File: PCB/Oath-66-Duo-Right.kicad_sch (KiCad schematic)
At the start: 67 parts, among them U2 Arduino_Pro_Micro

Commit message: PCB Updated
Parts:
- S52: footprint ScottoKeebs_Hotswap:Hotswap_MX_1.50u -> ScottoKeebs_Hotswap:Hotswap_MX_1.00u
- S53: footprint ScottoKeebs_Hotswap:Hotswap_MX_1.00u -> ScottoKeebs_Hotswap:Hotswap_MX_1.50u
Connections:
- net Col 0: no longer D48.1 (K), D49.1 (K), D50.1 (K), D51.1 (K), D52.1 (K), D53.1 (K), U2.12 (9/PB5)
- net Col 1: now also S62.1
- net Col 2: no longer S62.1
- new net Row 2: D48.1 (K), D49.1 (K), D50.1 (K), D51.1 (K), D52.1 (K), D53.1 (K), U2.12 (9/PB5)
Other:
- moved on the sheet: D62, S62
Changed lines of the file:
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@@
 	)
 	(junction
-		(at 189.23 101.6)
-		(diameter 0)
-		(color 0 0 0 0)
-	)
-	(junction
 		(at 234.95 48.26)
 		(diameter 0)
@@
 	)
 	(junction
-		(at 212.09 109.22)
-		(diameter 0)
-		(color 0 0 0 0)
-	)
-	(junction
 		(at 234.95 109.22)
 		(diameter 0)
@@
 	)
 	(junction
+		(at 200.66 109.22)
+		(diameter 0)
+		(color 0 0 0 0)
+	)
+	(junction
 		(at 240.03 121.92)
 		(diameter 0)
@@
 	)
 	(junction
+		(at 205.74 142.24)
+		(diameter 0)
+		(color 0 0 0 0)
+	)
+	(junction
 		(at 240.03 101.6)
 		(diameter 0)
@@
 	)
 	(junction
-		(at 217.17 142.24)
-		(diameter 0)
-		(color 0 0 0 0)
-	)
-	(junction
 		(at 234.95 68.58)
 		(diameter 0)
@@
 	)
 	(junction
-		(at 205.74 101.6)
-		(diameter 0)
-		(color 0 0 0 0)
-	)
-	(junction
 		(at 257.81 68.58)
 		(diameter 0)
@@
 	(wire
 		(pts
-			(xy 251.46 142.24) (xy 262.89 142.24)
+			(xy 200.66 109.22) (xy 200.66 129.54)
 		)
 		(stroke
@@
 	(wire
 		(pts
-			(xy 228.6 121.92) (xy 240.03 121.92)
+			(xy 251.46 142.24) (xy 262.89 142.24)
 		)
 		(stroke
@@
 	(wire
 		(pts
-			(xy 194.31 142.24) (xy 217.17 142.24)
+			(xy 228.6 121.92) (xy 240.03 121.92)
 		)
 		(stroke
@@
 	(wire
 		(pts
-			(xy 212.09 48.26) (xy 212.09 68.58)
+			(xy 194.31 142.24) (xy 205.74 142.24)
 		)
 		(stroke
@@
 	(wire
 		(pts
-			(xy 194.31 121.92) (xy 205.74 121.92)
+			(xy 212.09 48.26) (xy 212.09 68.58)
 		)
 		(stroke
@@
 	(wire
 		(pts
-			(xy 217.17 142.24) (xy 228.6 142.24)
+			(xy 194.31 121.92) (xy 205.74 121.92)
 		)
 		(stroke
@@
 	(wire
 		(pts
-			(xy 246.38 88.9) (xy 246.38 109.22)
+			(xy 205.74 142.24) (xy 228.6 142.24)
 		)
 		(stroke
@@
 	(wire
 		(pts
-			(xy 189.23 101.6) (xy 205.74 101.6)
+			(xy 246.38 88.9) (xy 246.38 109.22)
 		)
 		(stroke
@@
 	(wire
 		(pts
-			(xy 189.23 68.58) (xy 189.23 101.6)
-		)
-		(stroke
-			(width 0)
-			(type default)
-		)
-	)
-	(wire
-		(pts
 			(xy 88.9 62.23) (xy 86.36 62.23)
 		)
@@
 	(wire
 		(pts
-			(xy 189.23 101.6) (xy 189.23 109.22)
+			(xy 189.23 68.58) (xy 189.23 109.22)
 		)
 		(stroke
@@
 	(wire
 		(pts
-			(xy 212.09 109.22) (xy 212.09 129.54)
-		)
-		(stroke
-			(width 0)
-			(type default)
-		)
-	)
-	(wire
-		(pts
 			(xy 205.74 101.6) (xy 217.17 101.6)
 		)
@@
 	(symbol
 		(lib_id "ScottoKeebs:Placeholder_Keyswitch")
-		(at 214.63 132.08 0)
+		(at 203.2 132.08 0)
 		(unit 1)
 		(exclude_from_sim no)
@@
 		(fields_autoplaced yes)
 		(property "Reference" "S62"
-			(at 214.63 124.46 0)
+			(at 203.2 124.46 0)
 			(effects
 				(font
@@
 		)
 		(property "Value" "Keyswitch"
-			(at 214.63 127 0)
+			(at 203.2 127 0)
 			(effects
 				(font
@@
 		)
 		(property "Footprint" "ScottoKeebs_Hotswap:Hotswap_MX_2.00u"
-			(at 214.63 132.08 0)
+			(at 203.2 132.08 0)
 			(effects
 				(font
@@
 		)
 		(property "Datasheet" "~"
-			(at 214.63 132.08 0)
+			(at 203.2 132.08 0)
 			(effects
 				(font
@@
 		)
 		(property "Description" "Push button switch, normally open, two pins, 45° tilted"
-			(at 214.63 132.08 0)
+			(at 203.2 132.08 0)
 			(effects
 				(font
@@
 	(symbol
 		(lib_id "ScottoKeebs:Placeholder_Diode")
-		(at 217.17 138.43 90)
+		(at 205.74 138.43 90)
 		(unit 1)
 		(exclude_from_sim no)
@@
 		(fields_autoplaced yes)
 		(property "Reference" "D62"
-			(at 219.71 137.1599 90)
+			(at 208.28 137.1599 90)
 			(effects
 				(font
@@
 		)
 		(property "Value" "Diode"
-			(at 219.71 139.6999 90)
+			(at 208.28 139.6999 90)
 			(effects
 				(font
@@
 		)
 		(property "Footprint" "ScottoKeebs_Components:Diode_SOD-123"
-			(at 217.17 138.43 0)
+			(at 205.74 138.43 0)
 			(effects
 				(font
@@
 		)
 		(property "Datasheet" ""
-			(at 217.17 138.43 0)
+			(at 205.74 138.43 0)
 			(effects
 				(font
@@
 		)
 		(property "Description" "1N4148 (DO-35) or 1N4148W (SOD-123)"
-			(at 217.17 138.43 0)
+			(at 205.74 138.43 0)
 			(effects
 				(font
@@
 		)
 		(property "Sim.Device" "D"
-			(at 217.17 138.43 0)
+			(at 205.74 138.43 0)
 			(effects
 				(font
@@
 		)
 		(property "Sim.Pins" "1=K 2=A"
-			(at 217.17 138.43 0)
+			(at 205.74 138.43 0)
 			(effects
 				(font
@@
 			)
 		)
-		(property "Footprint" "ScottoKeebs_Hotswap:Hotswap_MX_1.00u"
+		(property "Footprint" "ScottoKeebs_Hotswap:Hotswap_MX_1.50u"
 			(at 260.35 91.44 0)
 			(effects
@@
 			)
 		)
-		(property "Footprint" "ScottoKeebs_Hotswap:Hotswap_MX_1.50u"
+		(property "Footprint" "ScottoKeebs_Hotswap:Hotswap_MX_1.00u"
 			(at 248.92 91.44 0)
 			(effects

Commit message: PCB Updated
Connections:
- net Col 0: now also U2.9 (6/PD7); no longer U2.8 (5/PC6)
- net Col 1: now also U2.20 (A3/PF4); no longer U2.10 (7/PE6)
- net Col 2: now also U2.18 (A1/PF6); no longer U2.11 (8/PB4)
- net Col 3: now also U2.16 (15/PB1); no longer U2.15 (14/PB3)
- net Col 4: now also U2.14 (16/PB2); no longer U2.13 (10/PB6)
- net Col 5: now also U2.12 (9/PB5); no longer U2.5 (2/PD1)
- net Col 6: now also U2.11 (8/PB4); no longer U2.6 (3/PD0)
- net Row 0: now also U2.10 (7/PE6); no longer U2.7 (4/PD4)
- net Row 1: now also U2.19 (A2/PF5); no longer U2.9 (6/PD7)
- net Row 2: now also U2.17 (A0/PF7); no longer U2.12 (9/PB5)
- net Row 3: now also U2.15 (14/PB3); no longer U2.16 (15/PB1)
- net Row 4: now also U2.13 (10/PB6); no longer U2.14 (16/PB2)

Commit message: PCB Updated
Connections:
- net Col 0: now also U2.10 (7/PE6); no longer U2.9 (6/PD7)
- net Col 1: now also U2.9 (6/PD7); no longer U2.20 (A3/PF4)
- net Col 2: now also U2.14 (16/PB2); no longer U2.18 (A1/PF6)
- net Col 4: now also U2.18 (A1/PF6); no longer U2.14 (16/PB2)
- net Col 5: now also U2.20 (A3/PF4); no longer U2.12 (9/PB5)
- net Row 0: now also U2.12 (9/PB5); no longer U2.10 (7/PE6)

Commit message: Schematic and PCB Updated
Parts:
- added H10, H6, H7, H8, H9: Mounting_Hole, MountingHole:MountingHole_2.5mm, symbol ScottoKeebs:Placeholder_Mounting_Hole
- added J2: Conn_01x02, Connector_JST:JST_PH_S2B-PH-K_1x02_P2.00mm_Horizontal, symbol Connector_Generic:Conn_01x02
- added PSW2: ~, MyLibrary:MSK_1134_3PIN_2H, symbol MyLibrary:MSK_1134_3PIN_2H
- added RSW2: ~, MyLibrary:Tactile_Switch_3_6_2.5mm, symbol MyLibrary:Tactile_Swtich_3*6*2.5mm
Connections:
- net BAT+_R: now reaches U2.21 (VCC)
- net BAT+_R: now also PSW2.2
- net RST_R: now reaches U2.22 (RST)
- net RST_R: now also RSW2.1
- net GND_R: now reaches U2.3 (GND)
- net GND_R: now also U2.4 (GND), J2.2 (Pin_2), RSW2.2
- net Col 0 renamed COL0_R
- net Col 1 renamed COL1_R
- net Col 2 renamed COL2_R
- net Col 3 renamed COL3_R
- net Col 4 renamed COL4_R
- net Col 5 renamed COL5_R
- net Col 6 renamed COL6_R
- net Row 0 renamed ROW0_R
- net Row 1 renamed ROW1_R
- net Row 2 renamed ROW2_R
- net Row 3 renamed ROW3_R
- net Row 4 renamed ROW4_R
- new net VBAT_R: J2.1 (Pin_1), PSW2.3
- no-connect marks 0 -> 9

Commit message: PCB Routing Finished
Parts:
- removed J2: Conn_01x02, Connector_JST:JST_PH_S2B-PH-K_1x02_P2.00mm_Horizontal, symbol Connector_Generic:Conn_01x02
- added J2: Connector_PH2.0_2Pin_Horizontal, Connector_JST:JST_GH_SM02B-GHS-TB_1x02-1MP_P1.25mm_Horizontal, symbol MyLibrary:Connector_PH2.0_2Pin_Horizontal
- PSW2: footprint MyLibrary:MSK_1134_3PIN_2H -> MyLibrary:MSK_1134_3Pin_2H; symbol MyLibrary:MSK_1134_3PIN_2H -> MyLibrary:MSK_1134_3Pin_2H
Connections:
- net GND_R: now also U2.23 (GND), J2.2 (Pin_2)
- net VBAT_R: now also J2.1 (Pin_1)
- no-connect marks 9 -> 10
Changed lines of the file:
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@@
 	)
 	(no_connect
-		(at 86.36 44.45)
-	)
-	(no_connect
 		(at 55.88 52.07)
 	)
@@
 	)
 	(no_connect
+		(at 139.7 93.98)
+	)
+	(no_connect
 		(at 146.05 55.88)
 	)
@@
 	)
 	(no_connect
+		(at 139.7 81.28)
+	)
+	(no_connect
 		(at 55.88 54.61)
 	)
@@
 	(wire
 		(pts
+			(xy 88.9 44.45) (xy 86.36 44.45)
+		)
+		(stroke
+			(width 0)
+			(type default)
+		)
+	)
+	(wire
+		(pts
 			(xy 234.95 109.22) (xy 234.95 129.54)
 		)
@@
 		)
 	)
+	(hierarchical_label "GND_R"
+		(shape input)
+		(at 88.9 44.45 0)
+		(effects
+			(font
+				(size 1.27 1.27)
+			)
+			(justify left)
+		)
+	)
 	(hierarchical_label "ROW0_R"
 		(shape input)
@@
 	)
 	(symbol
-		(lib_id "Connector_Generic:Conn_01x02")
-		(at 139.7 88.9 180)
-		(unit 1)
-		(exclude_from_sim no)
-		(in_bom yes)
-		(on_board yes)
-		(dnp no)
-		(fields_autoplaced yes)
-		(property "Reference" "J2"
-			(at 139.7 80.01 0)
-			(effects
-				(font
-					(size 1.27 1.27)
-				)
-			)
-		)
-		(property "Value" "Conn_01x02"
-			(at 139.7 82.55 0)
-			(effects
-				(font
-					(size 1.27 1.27)
-				)
-			)
-		)
-		(property "Footprint" "Connector_JST:JST_PH_S2B-PH-K_1x02_P2.00mm_Horizontal"
-			(at 139.7 88.9 0)
-			(effects
-				(font
-					(size 1.27 1.27)
-				)
-				(hide yes)
-			)
-		)
-		(property "Datasheet" "~"
-			(at 139.7 88.9 0)
-			(effects
-				(font
-					(size 1.27 1.27)
-				)
-				(hide yes)
-			)
-		)
-		(property "Description" "Generic connector, single row, 01x02, script generated (kicad-library-utils/schlib/autogen/connector/)"
-			(at 139.7 88.9 0)
-			(effects
-				(font
-					(size 1.27 1.27)
-				)
-				(hide yes)
-			)
-		)
-		(pin "1"
-		)
-		(pin "2"
-		)
-		(instances
-			(project "Oath-66-Duo"
-				(path "/79e2eb2a-25a9-43ec-81b5-27be6f17dde1/f5aa2fbd-50f4-4620-8b87-71987b807485"
-					(reference "J2")
-					(unit 1)
-				)
-			)
-		)
-	)
-	(symbol
 		(lib_id "ScottoKeebs:Placeholder_Mounting_Hole")
 		(at 152.4 127 0)
@@
 	)
 	(symbol
+		(lib_id "MyLibrary:Connector_PH2.0_2Pin_Horizontal")
+		(at 140.97 87.63 180)
+		(unit 1)
+		(exclude_from_sim no)
+		(in_bom yes)
+		(on_board yes)
+		(dnp no)
+		(fields_autoplaced yes)
+		(property "Reference" "J2"
+			(at 137.16 86.3599 0)
+			(effects
+				(font
+					(size 1.27 1.27)
+				)
+				(justify left)
+			)
+		)
+		(property "Value" "Connector_PH2.0_2Pin_Horizontal"
+			(at 137.16 88.8999 0)
+			(effects
+				(font
+					(size 1.27 1.27)
+				)
+				(justify left)
+			)
+		)
+		(property "Footprint" "Connector_JST:JST_GH_SM02B-GHS-TB_1x02-1MP_P1.25mm_Horizontal"
+			(at 140.97 87.63 0)
+			(effects
+				(font
+					(size 1.27 1.27)
+				)
+				(hide yes)
+			)
+		)
+		(property "Datasheet" ""
+			(at 140.97 87.63 0)
+			(effects
+				(font
+					(size 1.27 1.27)
+				)
+				(hide yes)
+			)
+		)
+		(property "Description" "PH2.0接插件2PIN卧贴"
+			(at 141.224 74.93 0)
+			(effects
+				(font
+					(size 1.27 1.27)
+				)
+				(hide yes)
+			)
+		)
+		(pin "MP"
+		)
+		(pin "2"
+		)
+		(pin "MP"
+		)
+		(pin "1"
+		)
+		(instances
+			(project "Oath-66-Duo"
+				(path "/79e2eb2a-25a9-43ec-81b5-27be6f17dde1/f5aa2fbd-50f4-4620-8b87-71987b807485"
+					(reference "J2")
+					(unit 1)
+				)
+			)
+		)
+	)
+	(symbol
 		(lib_id "ScottoKeebs:Placeholder_Diode")
 		(at 228.6 97.79 90)
@@
 	)
 	(symbol
-		(lib_id "MyLibrary:MSK_1134_3PIN_2H")
+		(lib_id "MyLibrary:MSK_1134_3Pin_2H")
 		(at 139.7 58.42 0)
 		(unit 1)
@@
 			)
 		)
-		(property "Footprint" "MyLibrary:MSK_1134_3PIN_2H"
+		(property "Footprint" "MyLibrary:MSK_1134_3Pin_2H"
 			(at 139.7 68.326 0)
 			(effects

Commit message: Bug Fixed
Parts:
- removed U2: Arduino_Pro_Micro, ScottoKeebs_MCU:Arduino_Pro_Micro, symbol ScottoKeebs:MCU_Arduino_Pro_Micro
- added U2: nice_nano, PCM_marbastlib-xp-promicroish:nice_nano_AH_USBup, symbol PCM_marbastlib-promicroish:nice_nano
- J2: value Connector_PH2.0_2Pin_Horizontal -> GH1.25 Battery Connector
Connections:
- net BAT+_R: now also U2.29 (BAT+)
- net COL0_R: now also U2.10 (P0.11)
- net COL1_R: now also U2.9 (P1.00)
- net COL2_R: now also U2.23 (P0.10-LF)
- net COL3_R: now also U2.21 (P1.13-LF)
- net COL4_R: now also U2.19 (P0.02-LF)
- net COL5_R: now also U2.17 (P0.31-LF)
- net COL6_R: now also U2.11 (P1.04-LF)
- net GND_R: now also U2.14 (GND), U2.28 (GND), U2.3 (GND), U2.4 (GND)
- net ROW0_R: now also U2.12 (P1.06-LF)
- net ROW1_R: now also U2.18 (P0.29-LF)
- net ROW2_R: now also U2.20 (P1.15-LF)
- net ROW3_R: now also U2.22 (P1.11-LF)
- net ROW4_R: now also U2.24 (P0.09-LF)
- net RST_R: now also U2.15 (RST)
- no-connect marks 10 -> 13
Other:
- note added: "Battery Connector and Power Switch"
- note added: "Mounting Hole"
- note added: "Nice Nano V2"
- note added: "Oath 66 Duo"
- note added: "Reset Button"
- note added: "with dongle"
- moved on the sheet: H10, H6, H7, H8, H9, PSW2, RSW2

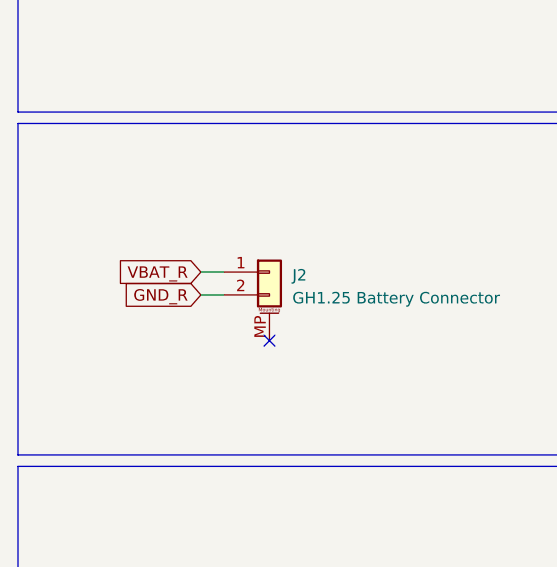
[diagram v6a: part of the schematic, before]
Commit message: Battery Connector Updated
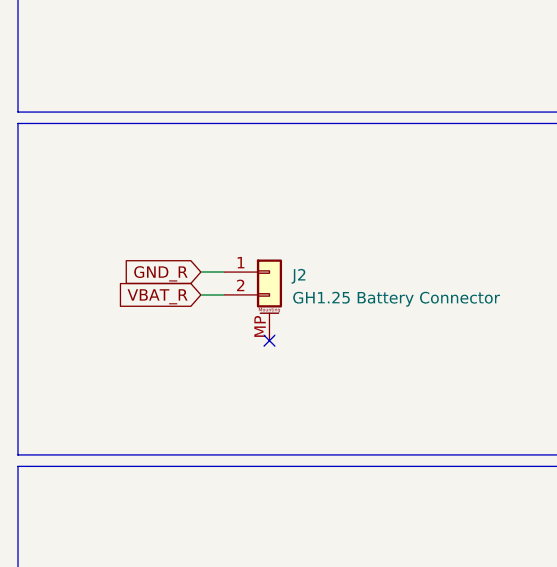
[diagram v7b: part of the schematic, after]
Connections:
- net GND_R: now also J2.1 (Pin_1); no longer J2.2 (Pin_2)
- net VBAT_R: now also J2.2 (Pin_2); no longer J2.1 (Pin_1)
